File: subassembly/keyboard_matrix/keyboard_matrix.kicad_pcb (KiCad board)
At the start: 2 copper layers, 150 x 100 mm, 76 parts, among them J10 Data, J11 Debug, Q101 2N7002, SW201 Keyswitch-SK6812Mini-E, SW202 Keyswitch-SK6812Mini-E, SW203 Keyswitch-SK6812Mini-E, SW204 Keyswitch-SK6812Mini-E, SW205 Keyswitch-SK6812Mini-E, SW206 Keyswitch-SK6812Mini-E, SW207 Keyswitch-SK6812Mini-E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

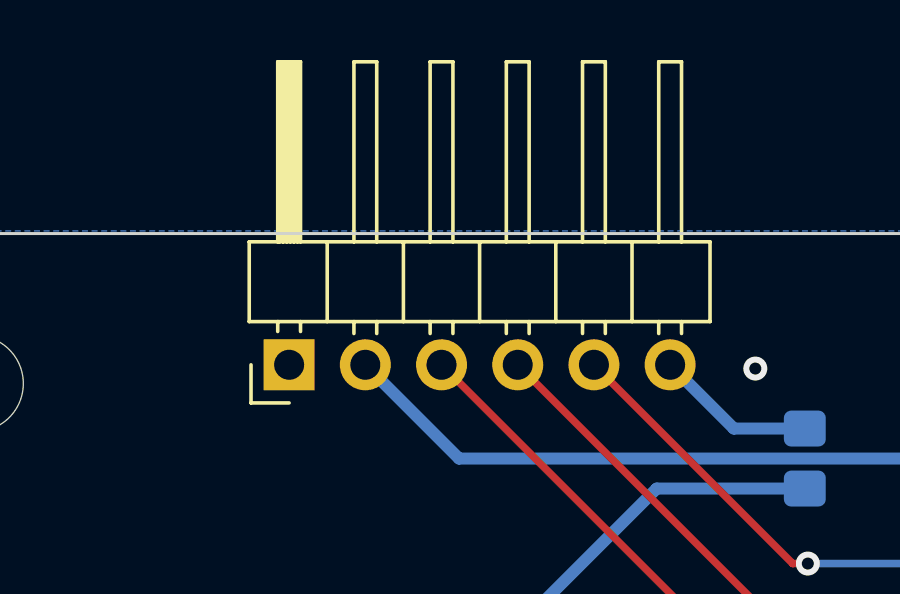
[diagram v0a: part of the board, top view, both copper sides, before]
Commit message: First run of keyboard board and move prototype board to rotary_encoder_board
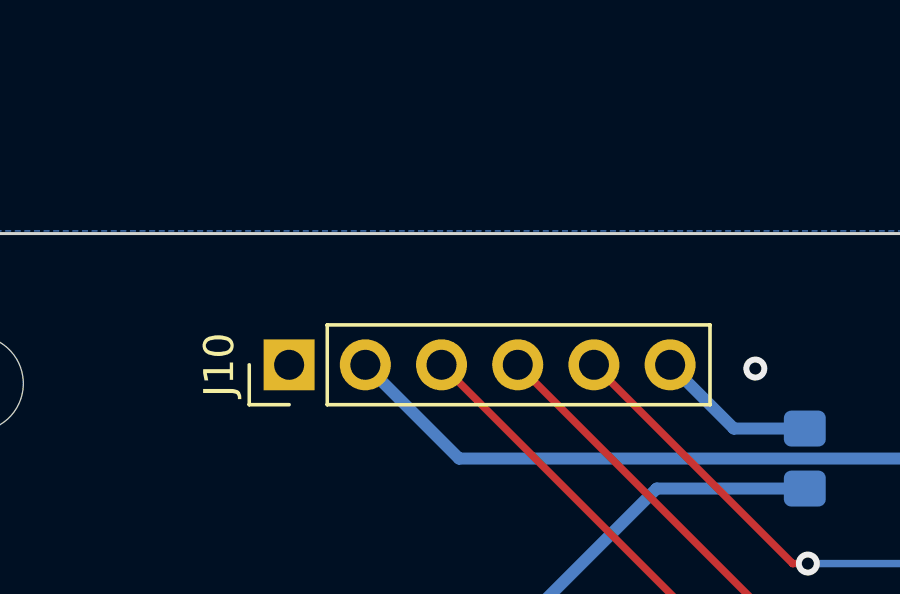
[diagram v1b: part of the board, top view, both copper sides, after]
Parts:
- J10: footprint Connector_PinHeader_2.54mm:PinHeader_1x06_P2.54mm_Horizontal -> Connector_PinHeader_2.54mm:PinHeader_1x06_P2.54mm_Vertical
